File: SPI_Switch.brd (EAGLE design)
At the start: 100 x 80 mm, 36 parts, among them J1 8516-4500PL, J2 1-406525-1, J3 1-406525-1, J4 0705510037, J5 0705510037, U1 TLE7230G, U2 SN74ABT126

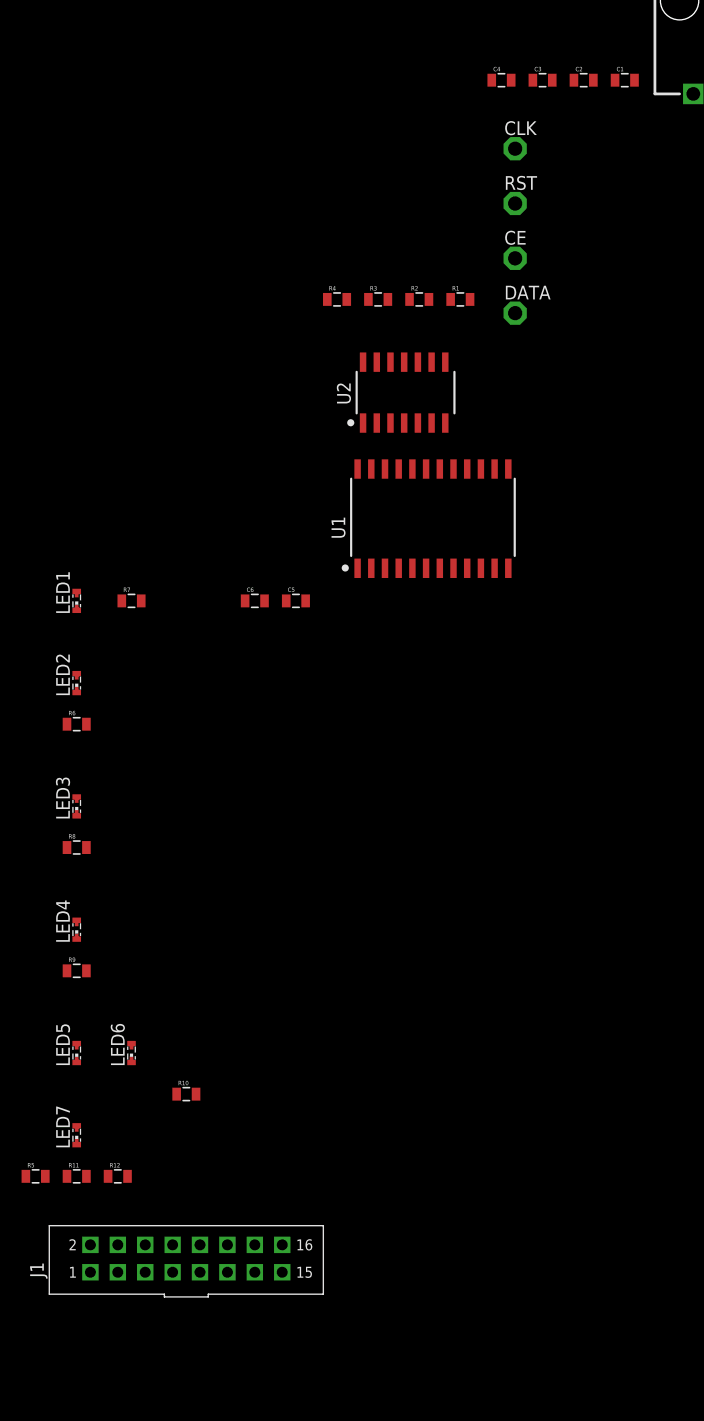
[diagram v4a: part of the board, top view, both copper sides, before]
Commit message: Adding part numbers
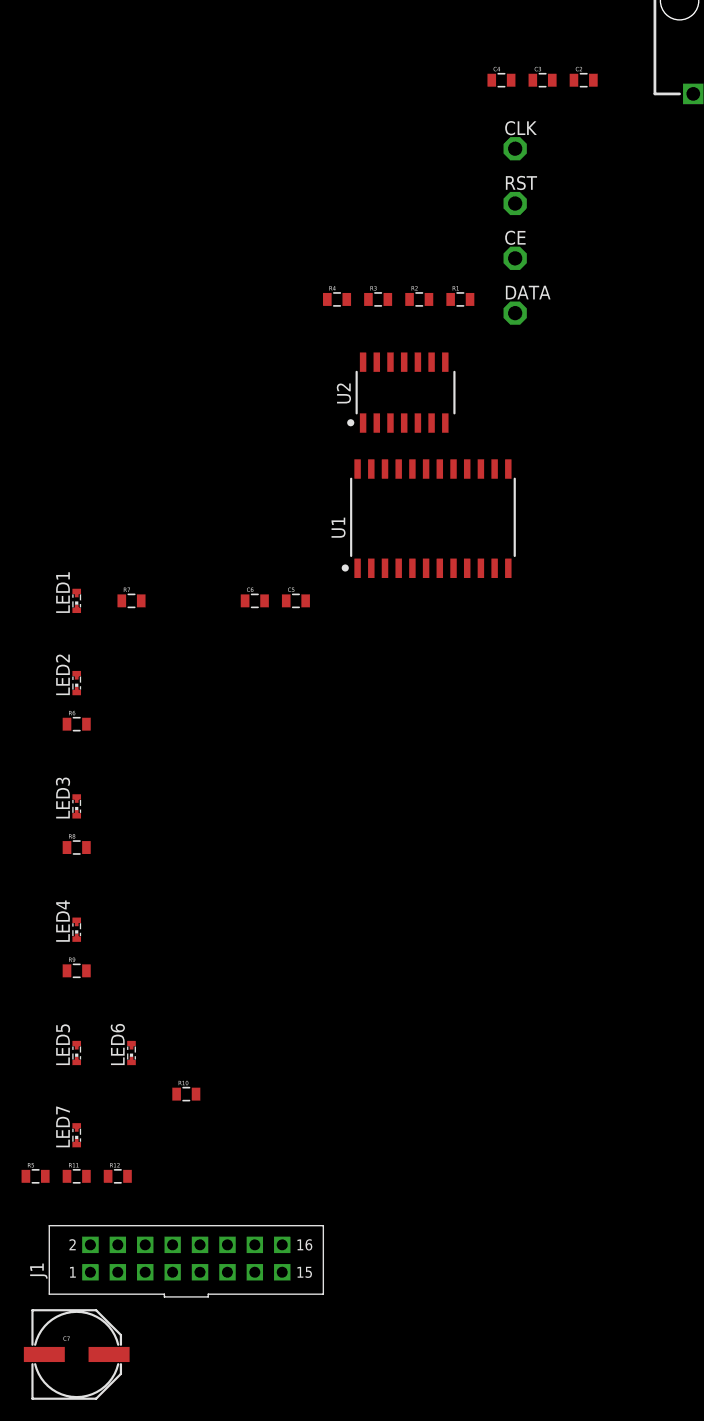
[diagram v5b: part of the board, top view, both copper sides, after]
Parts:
- removed C1: 220uF electrolytic, SparkFun-Passives:0805
- added C7: 220uF, SparkFun-Passives:PANASONIC_E
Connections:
- net +24V: now also C7.+; no longer C1.1
- net GND: now also C7.-; no longer C1.2
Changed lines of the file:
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@@
 <element name="J2" library="SPI_Switch" package="1-406525-1" value="1-406525-1" x="1.27" y="-48.26"/>
 <element name="J4" library="SPI_Switch" package="0705510037" value="0705510037" x="-22.86" y="-50.8"/>
-<element name="C1" library="SparkFun-Passives" package="0805" value="220uF electrolytic" x="-29.21" y="-49.53"/>
 <element name="C2" library="SparkFun-Passives" package="0805" value="47uF" x="-33.02" y="-49.53"/>
 <element name="C3" library="SparkFun-Passives" package="0805" value="10uF" x="-36.83" y="-49.53"/>
@@
 <element name="R5" library="SparkFun-Passives" package="0805" value="1k" x="-83.82" y="-151.13"/>
 <element name="J1" library="SPI_Switch" package="8516-4500PL" value="8516-4500PL" x="-78.74" y="-160.02"/>
+<element name="C7" library="SparkFun-Passives" package="PANASONIC_E" value="220uF" x="-80.01" y="-167.64"/>
 </elements>
 <signals>
@@
 <contactref element="J5" pad="P$3"/>
 <contactref element="J4" pad="P$3"/>
-<contactref element="C1" pad="2"/>
 <contactref element="C2" pad="2"/>
 <contactref element="C4" pad="2"/>
@@
 <contactref element="U1" pad="2"/>
 <contactref element="J1" pad="P$15"/>
+<contactref element="C7" pad="-"/>
+<wire x1="-60.96" y1="-160.02" x2="-83.01" y2="-167.64" width="0" layer="19" extent="1-1"/>
 <wire x1="-62.6" y1="-97.79" x2="-60.96" y2="-160.02" width="0" layer="19" extent="1-1"/>
 <wire x1="-58.79" y1="-97.79" x2="-62.6" y2="-97.79" width="0" layer="19" extent="1-1"/>
@@
 <wire x1="-35.93" y1="-49.53" x2="-39.74" y2="-49.53" width="0" layer="19" extent="1-1"/>
 <wire x1="-32.12" y1="-49.53" x2="-35.93" y2="-49.53" width="0" layer="19" extent="1-1"/>
-<wire x1="-28.31" y1="-49.53" x2="-32.12" y2="-49.53" width="0" layer="19" extent="1-1"/>
-<wire x1="-17.78" y1="-50.8" x2="-28.31" y2="-49.53" width="0" layer="19" extent="1-1"/>
+<wire x1="-17.78" y1="-50.8" x2="-32.12" y2="-49.53" width="0" layer="19" extent="1-1"/>
 <wire x1="-4.826" y1="-48.26" x2="-17.78" y2="-50.8" width="0" layer="19" extent="1-1"/>
 <wire x1="-2.794" y1="-48.26" x2="-4.826" y2="-48.26" width="0" layer="19" extent="1-1"/>
@@
 <contactref element="J5" pad="P$1"/>
 <contactref element="J4" pad="P$1"/>
-<contactref element="C1" pad="1"/>
 <contactref element="R7" pad="1"/>
 <contactref element="R6" pad="1"/>
@@
 <contactref element="R5" pad="1"/>
 <contactref element="J1" pad="P$1"/>
+<contactref element="C7" pad="+"/>
+<wire x1="-78.74" y1="-160.02" x2="-77.01" y2="-167.64" width="0" layer="19" extent="1-1"/>
 <wire x1="-77.1" y1="-151.13" x2="-78.74" y2="-160.02" width="0" layer="19" extent="1-1"/>
 <wire x1="-80.91" y1="-151.13" x2="-77.1" y2="-151.13" width="0" layer="19" extent="1-1"/>
@@
 <wire x1="-80.91" y1="-109.22" x2="-80.91" y2="-120.65" width="0" layer="19" extent="1-1"/>
 <wire x1="-75.83" y1="-97.79" x2="-80.91" y2="-109.22" width="0" layer="19" extent="1-1"/>
-<wire x1="-30.11" y1="-49.53" x2="-75.83" y2="-97.79" width="0" layer="19" extent="1-1"/>
-<wire x1="-22.86" y1="-50.8" x2="-30.11" y2="-49.53" width="0" layer="19" extent="1-1"/>
+<wire x1="-22.86" y1="-50.8" x2="-75.83" y2="-97.79" width="0" layer="19" extent="1-1"/>
 <wire x1="-8.89" y1="-15.24" x2="-22.86" y2="-50.8" width="0" layer="19" extent="1-1"/>
 </signal>

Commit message: finished BOM
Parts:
- added LED8, LED9: YELLOW, SparkFun-LED:LED-1206
- added R13: 2k, SparkFun-Passives:R2512
- added R14: 330, SparkFun-Passives:0805
- LED1, LED2, LED3, LED4, LED5, LED6, LED7: device led:SMARTLED-TTW -> SparkFun-LED:LED-1206
- R10, R11, R12, R5, R6, R7, R8, R9: value 1k -> 2k; device SparkFun-Passives:0805 -> SparkFun-Passives:R2512
- moved R7 152.5 mm to (-80.0, -250.2)
- moved R12 137.2 mm to (-80.0, -288.3)
- moved R8 137.2 mm to (-80.0, -257.8)
- moved R6 133.3 mm to (-80.0, -242.6)
- moved R9 133.3 mm to (-80.0, -265.4)
- moved R10 129.9 mm to (-80.0, -273.1)
- moved R11 129.5 mm to (-80.0, -280.7)
- moved LED1 100.4 mm to (-82.5, -198.1)
- moved LED2 96.6 mm to (-82.5, -201.9)
- moved LED3 88.9 mm to (-82.5, -205.7)
- moved R5 83.9 mm to (-80.0, -234.9)
- moved LED4 81.3 mm to (-82.5, -209.6)
- moved LED6 77.8 mm to (-82.5, -217.2)
- moved LED5 73.7 mm to (-82.5, -213.4)
- moved LED7 73.7 mm to (-82.5, -221.0)
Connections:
- new net N$2: LED8.A, R5.1
- new net N$4: LED9.A, R14.1
- net +24V: now also R10.2, R11.2, R12.2, R13.2, R5.2, R6.2, R7.2, R8.2, R9.2; no longer R10.1, R11.1, R12.1, R5.1, R6.1, R7.1, R8.1, R9.1
- net +5V: now also R14.2
- net CH1: now also LED1.C; no longer LED1.C@1
- net CH2: now also LED2.C; no longer LED2.C@1
- net CH3: now also LED3.C; no longer LED3.C@1
- net CH4: now also LED4.C; no longer LED4.C@1
- net CH5: now also LED5.C; no longer LED5.C@1
- net CH6: now also LED6.C; no longer LED6.C@1
- net CH7: now also LED7.C; no longer LED7.C@1
- net CH8: now also R13.1; no longer R5.2
- net GND: now also LED8.C, LED9.C
- net N$1: now also LED1.A, R6.1; no longer LED1.A@1, R7.2
- net N$11: now also LED6.A, R11.1; no longer LED6.A@1, R11.2
- net N$13: now also LED7.A, R12.1; no longer LED7.A@1, R12.2
- net N$3: now also LED2.A, R7.1; no longer LED2.A@1, R6.2
- net N$5: now also LED3.A, R8.1; no longer LED3.A@1, R8.2
- net N$7: now also LED4.A, R9.1; no longer LED4.A@1, R9.2
- net N$9: now also LED5.A, R10.1; no longer LED5.A@1, R10.2

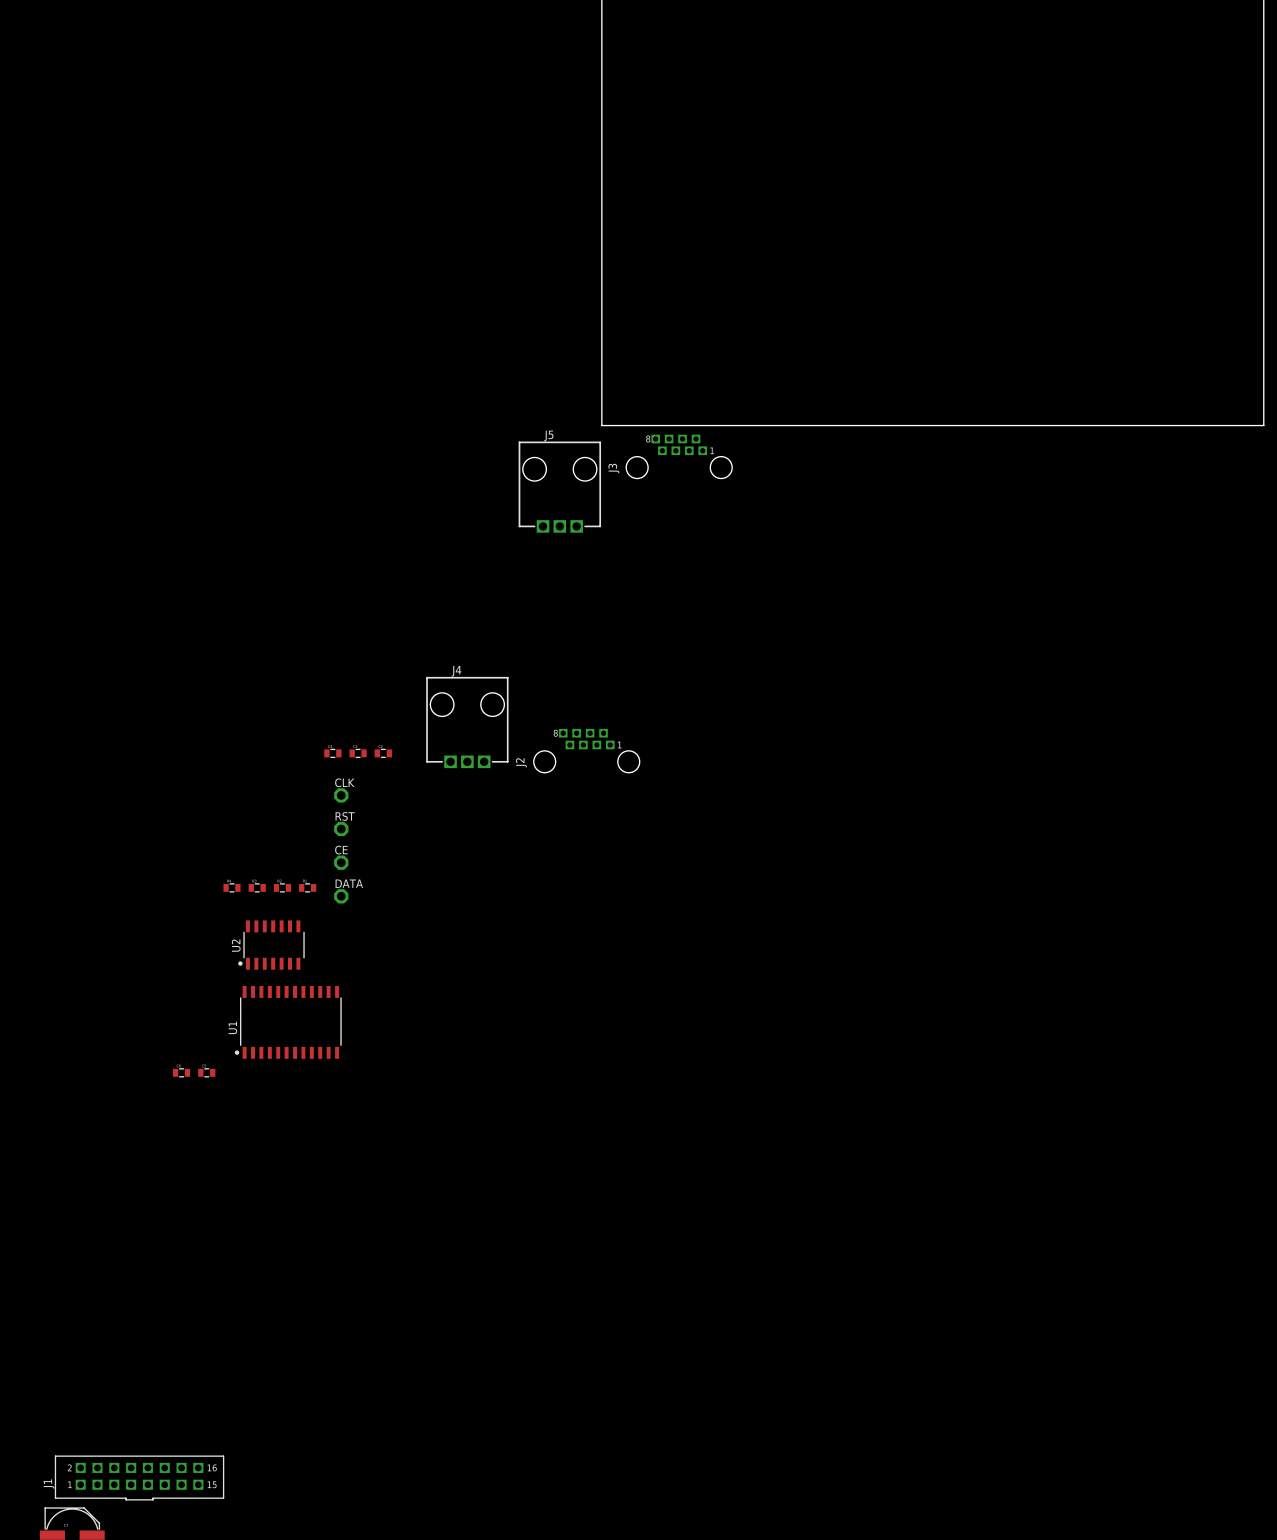
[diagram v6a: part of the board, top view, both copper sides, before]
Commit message: preliminary layout
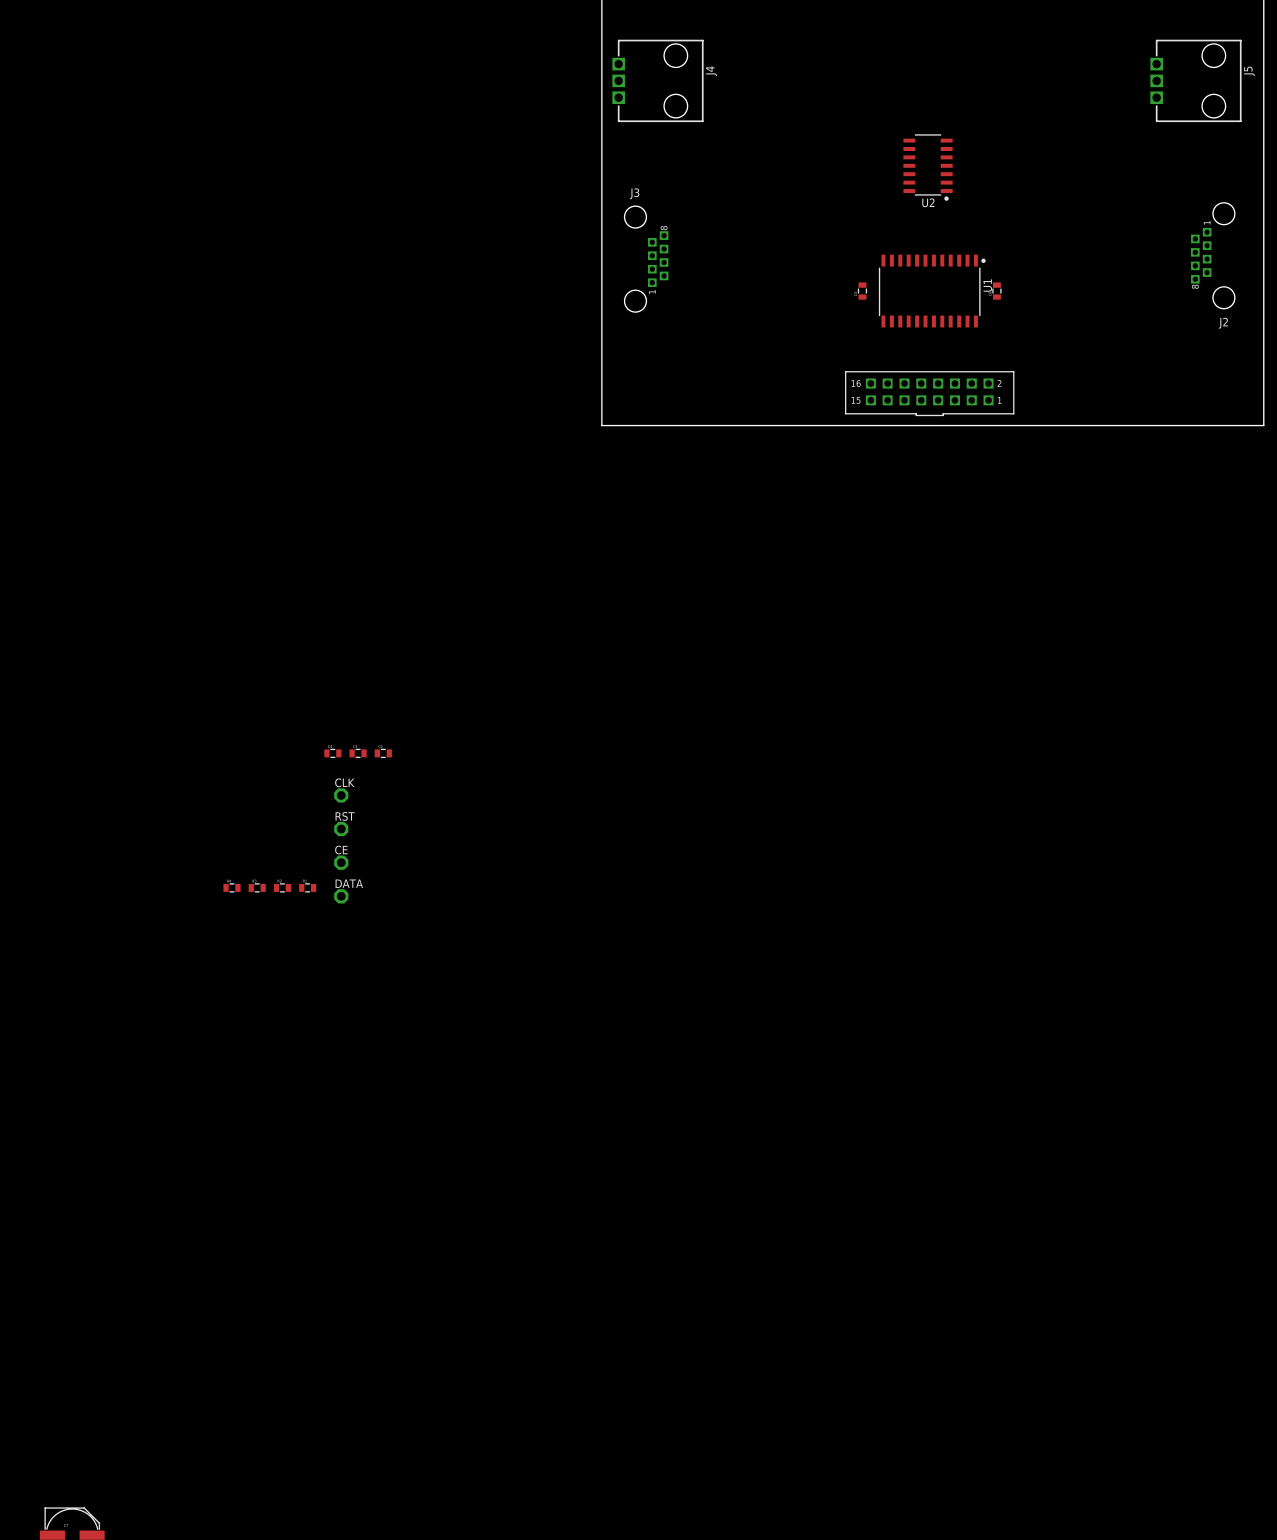
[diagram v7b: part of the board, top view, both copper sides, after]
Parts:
- moved J1 213.7 mm to (58.4, 3.81), flipped to the bottom
- moved U1 173.5 mm to (59.7, 29.2), turned to 180 degrees
- moved C6 170.7 mm to (59.7, 20.3), turned to 90 degrees
- moved U2 159.1 mm to (53.3, 34.3), turned to 90 degrees
- moved C5 154.2 mm to (39.4, 20.3), turned to 90 degrees
- moved J2 118.9 mm to (91.4, 29.2), turned to 90 degrees
- moved J5 116.1 mm to (83.8, 54.6), turned to 270 degrees
- moved J4 108.4 mm to (2.54, 54.6), turned to 270 degrees
- moved J3 26.5 mm to (7.62, 21.6), turned to 270 degrees

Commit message: Finished layout, must do routing now
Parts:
- moved R13 374.8 mm to (55.4, 53.6), turned to 90 degrees
- moved R12 351.3 mm to (18.0, 49.0), turned to 270 degrees
- moved R11 345.3 mm to (22.6, 49.0), turned to 270 degrees
- moved R10 339.4 mm to (27.2, 49.0), turned to 270 degrees
- moved R9 333.7 mm to (31.8, 49.0), turned to 270 degrees
- moved R14 333.0 mm to (11.9, 20.6)
- moved R8 328.1 mm to (36.3, 49.0), turned to 270 degrees
- moved R7 322.6 mm to (40.6, 49.0), turned to 270 degrees
- moved R6 317.2 mm to (45.0, 49.0), turned to 270 degrees
- moved LED7 295.3 mm to (18.0, 56.6), turned to 90 degrees
- moved LED6 293.3 mm to (22.6, 56.6), turned to 90 degrees
- moved LED5 291.4 mm to (27.2, 56.6), turned to 90 degrees
- moved LED4 289.7 mm to (31.8, 56.6), turned to 90 degrees
- moved LED3 288.1 mm to (36.3, 56.6), turned to 90 degrees
- moved LED2 286.4 mm to (40.6, 56.6), turned to 270 degrees
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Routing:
- net CLK: track 0.00 -> 64.8 mm
- net DATA_IN: track 0.00 -> 55.6 mm
- net CLK_POST: track 0.00 -> 21.5 mm
- net CE: track 0.00 -> 4.62 mm
- net RST_POST: track 0.00 -> 4.50 mm
- net RST: track 0.00 -> 4.50 mm
- net DATA_OUT: track 0.00 -> 4.00 mm
- net DATA_OUT_POST: track 0.00 -> 3.99 mm
- net CE_POST: track 0.00 -> 3.97 mm
